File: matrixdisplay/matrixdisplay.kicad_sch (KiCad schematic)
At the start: 93 parts, among them J1 FILAS, J2 COLUMNAS, J3 SWD, J4 USART, J5 FILAS, J6 COL, SW2 P_ON, SW3 BT1, SW4 BT2, U1 STM32F051K8Ux

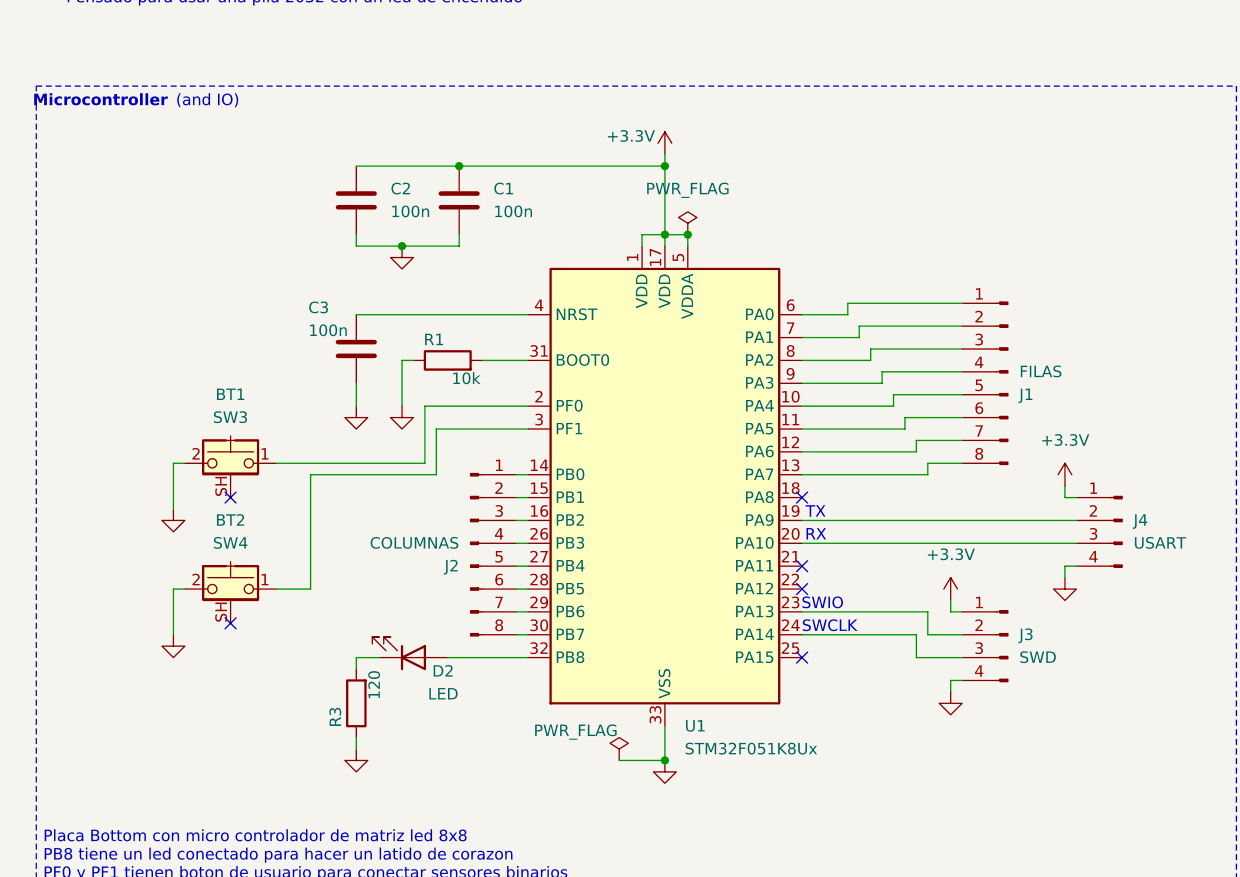
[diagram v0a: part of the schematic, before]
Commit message: feat(matrixdisplay): update components to exclude from BOM and save components 3D bodies
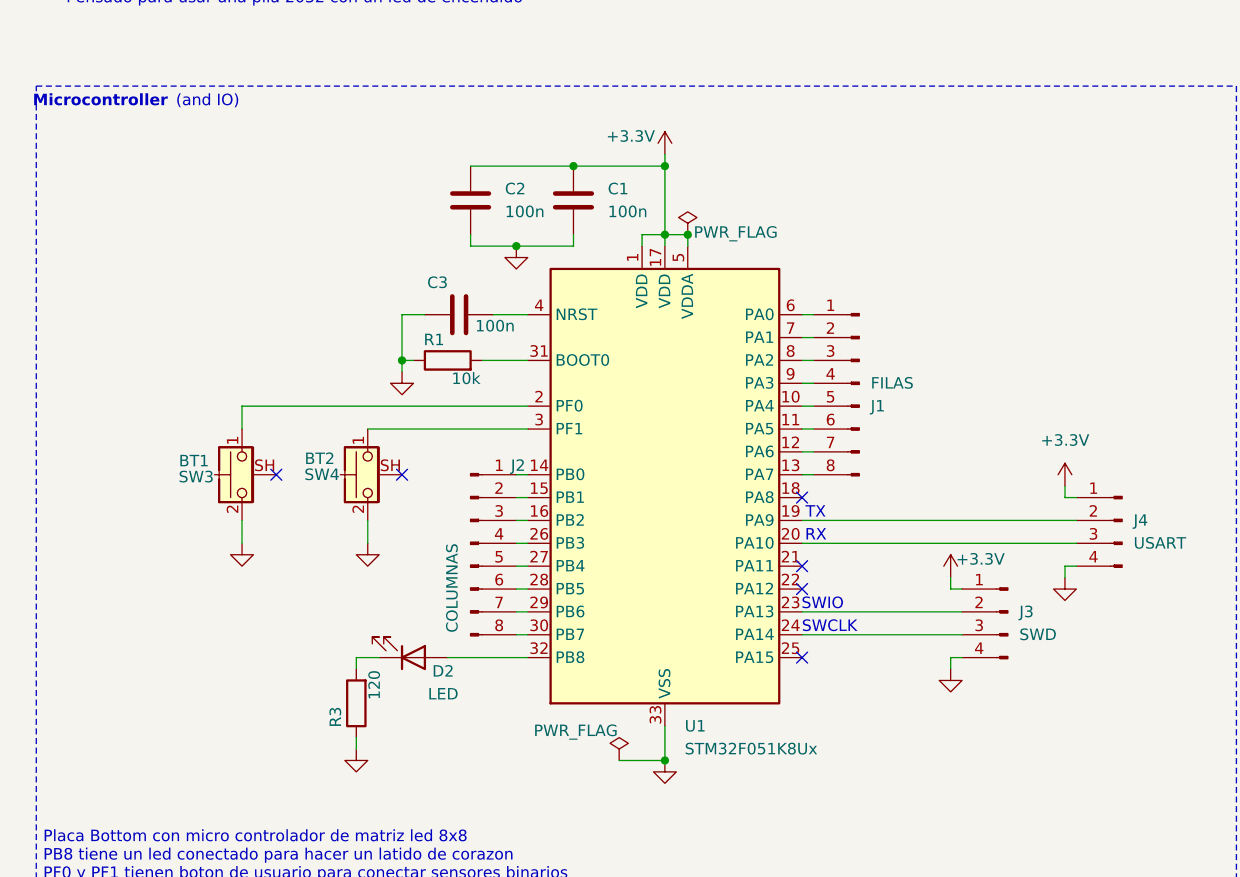
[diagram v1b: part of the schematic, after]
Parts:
- BT1, J1, J2, J3, J4, J5, J6: now left out of the parts list
- D1, D10, D11, D12, D13, D14, D15, D16, D17, D18, D19, D2, D20, D21, D22, D23, D24, D25, D26, D27, D28, D29, D3, D30, D31, D32, D33, D34, D35, D36, D37, D38, D39, D4, D40, D41, D42, D43, D44, D45, D46, D47, D48, D49, D5, D50, D51, D52, D53, D54, D55, D56, D57, D58, D59, D6, D60, D61, D62, D63, D64, D65, D66, D7, D8, D9: Manufacturer Part # (none) -> BL-HJC36G-AV-TRB
- SW2: Manufacturer Part # (none) -> MSK12C02
- SW3, SW4: Manufacturer Part # (none) -> TS24CAC393942
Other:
- moved on the sheet: C1, C2, C3, J1, J3, SW3, SW4

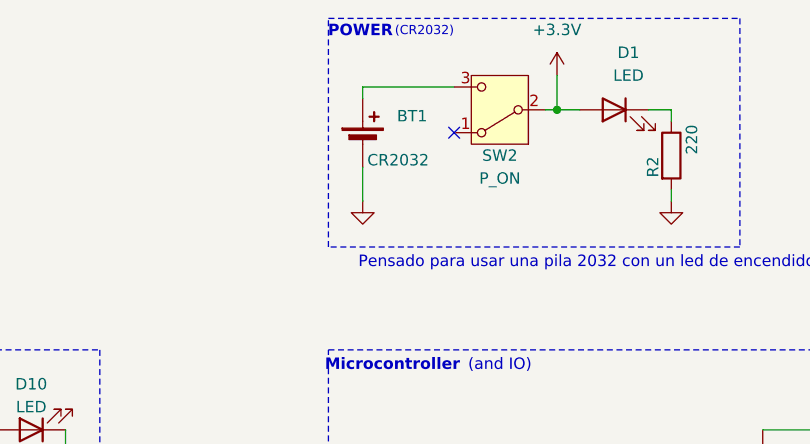
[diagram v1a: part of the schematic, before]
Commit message: feat(power): change battery footprint to match 2450 size
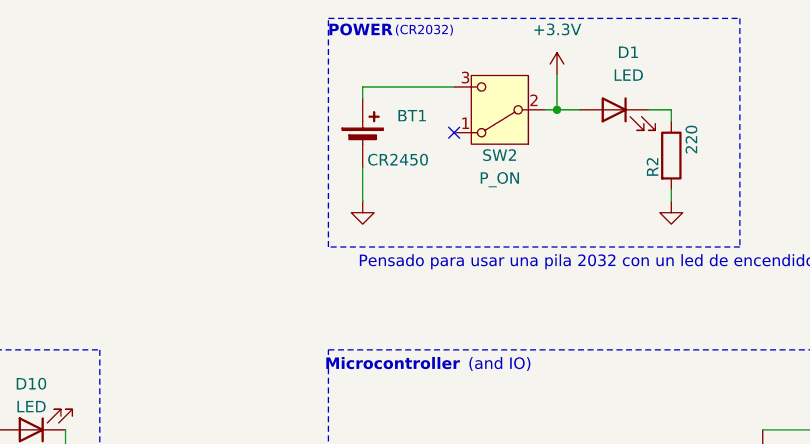
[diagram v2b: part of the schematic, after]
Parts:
- BT1: value CR2032 -> CR2450; footprint Battery:BatteryHolder_MYOUNG_BS-07-A1BJ001_CR2032 -> Battery:BatteryHolder_ComfortableElectronic_CH273-2450_1x2450
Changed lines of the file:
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@@
 			)
 		)
-		(property "Value" "CR2032"
+		(property "Value" "CR2450"
 			(at 152.908 32.258 0)
 			(effects
@@
 			)
 		)
-		(property "Footprint" "Battery:BatteryHolder_MYOUNG_BS-07-A1BJ001_CR2032"
+		(property "Footprint" "Battery:BatteryHolder_ComfortableElectronic_CH273-2450_1x2450"
 			(at 152.4 28.956 90)
 			(effects

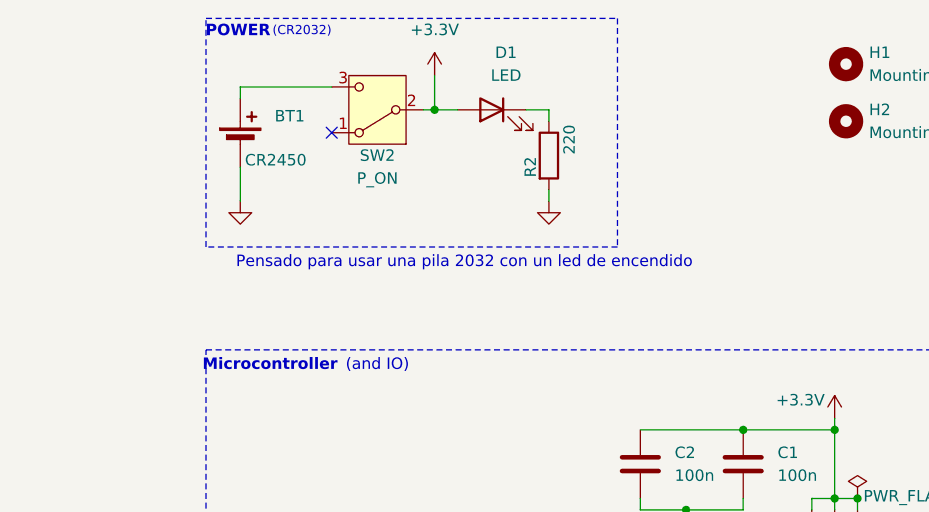
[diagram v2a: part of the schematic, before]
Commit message: feat(sch): remove stand by led and update text info
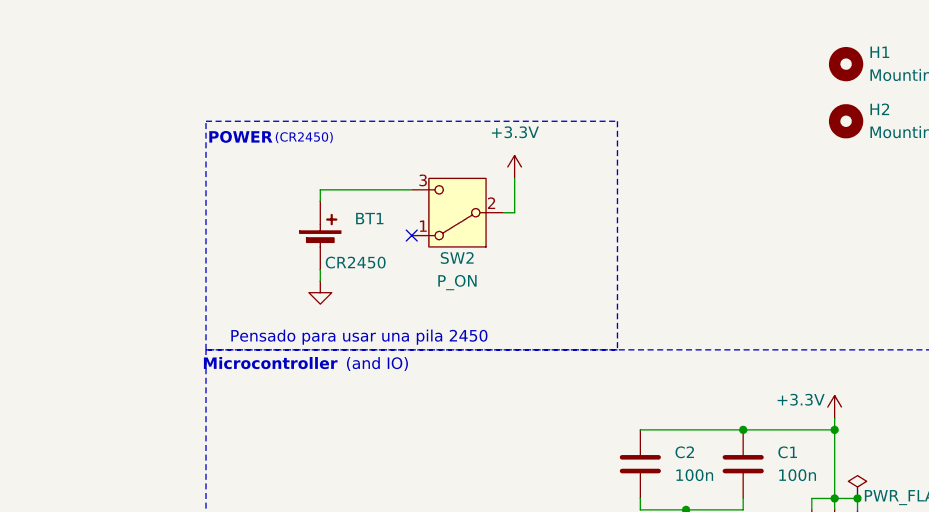
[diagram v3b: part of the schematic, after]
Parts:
- removed D1: LED, LED_SMD:LED_0603_1608Metric, symbol Device:LED
- removed R2: 220, Resistor_SMD:R_0603_1608Metric, symbol Device:R
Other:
- note added: "(CR2450)"
- note added: "Pensado para usar una pila 2450"
- note removed: "(CR2032)"
- note removed: "Pensado para usar una pila 2032 con un led de encendido"
- moved on the sheet: BT1, SW2
